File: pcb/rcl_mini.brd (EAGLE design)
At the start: 83.8 x 64.4 mm, 60 parts, among them CN1 USB mini B, Q1 8MHz, Q2 IRLML5203, U1 MCP6002T-I/SN, U2 MCP6002T-I/SN, U3 MCP6002T-I/SN, U4 STM32F100CBT6, U5 MCP73831/OT, U6 MCP1703CB, X1 BAT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

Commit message: pcb v1.0
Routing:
- net GND: track 474.3 -> 493.9 mm
- net VDD: track 138.5 -> 146.2 mm
- net HCUR: track 4.98 -> 10.8 mm
- net LCUR: track 5.10 -> 10.5 mm
- net LPOT: track 11.8 -> 16.9 mm
- net SWDIO: track 26.8 -> 31.9 mm
- net SWCLK: track 36.2 -> 41.2 mm
- net VBAT+: track 36.4 -> 40.2 mm
- net HPOT: track 11.5 -> 15.2 mm
- net OLED_I2C_SDA: track 28.3 -> 30.8 mm
- net OLED_I2C_SCK: track 34.3 -> 36.8 mm
- net UART_TX: track 24.3 -> 26.8 mm
- net UART_RX: track 24.5 -> 27.0 mm
- net SW3: track 21.0 -> 23.5 mm
- net SW1: track 25.7 -> 27.4 mm
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
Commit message: pcb v1.0 completed
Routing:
- net GND: track 493.9 -> 527.9 mm
- net HCUR2: track 17.4 -> 23.5 mm
- net USB+: track 23.2 -> 22.5 mm

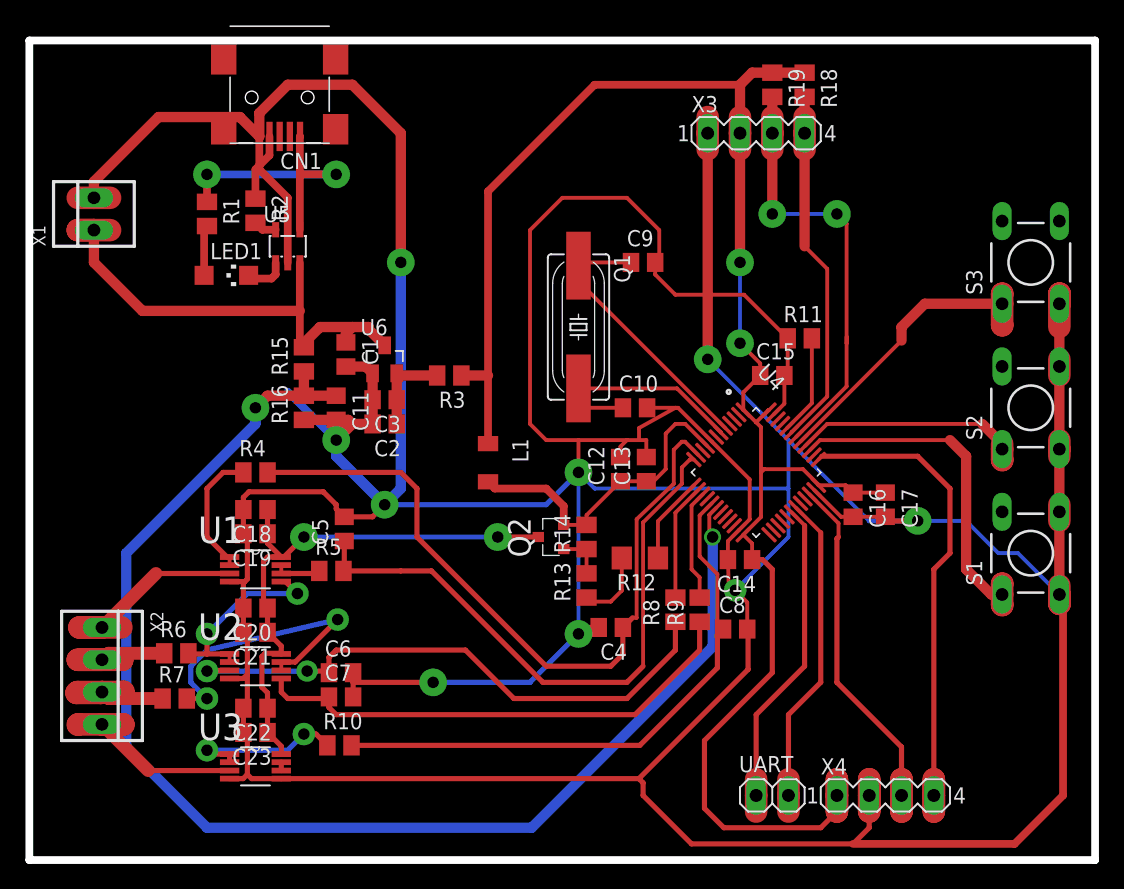
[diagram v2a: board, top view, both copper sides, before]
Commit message: mcp6002 package was changed from msop to soic
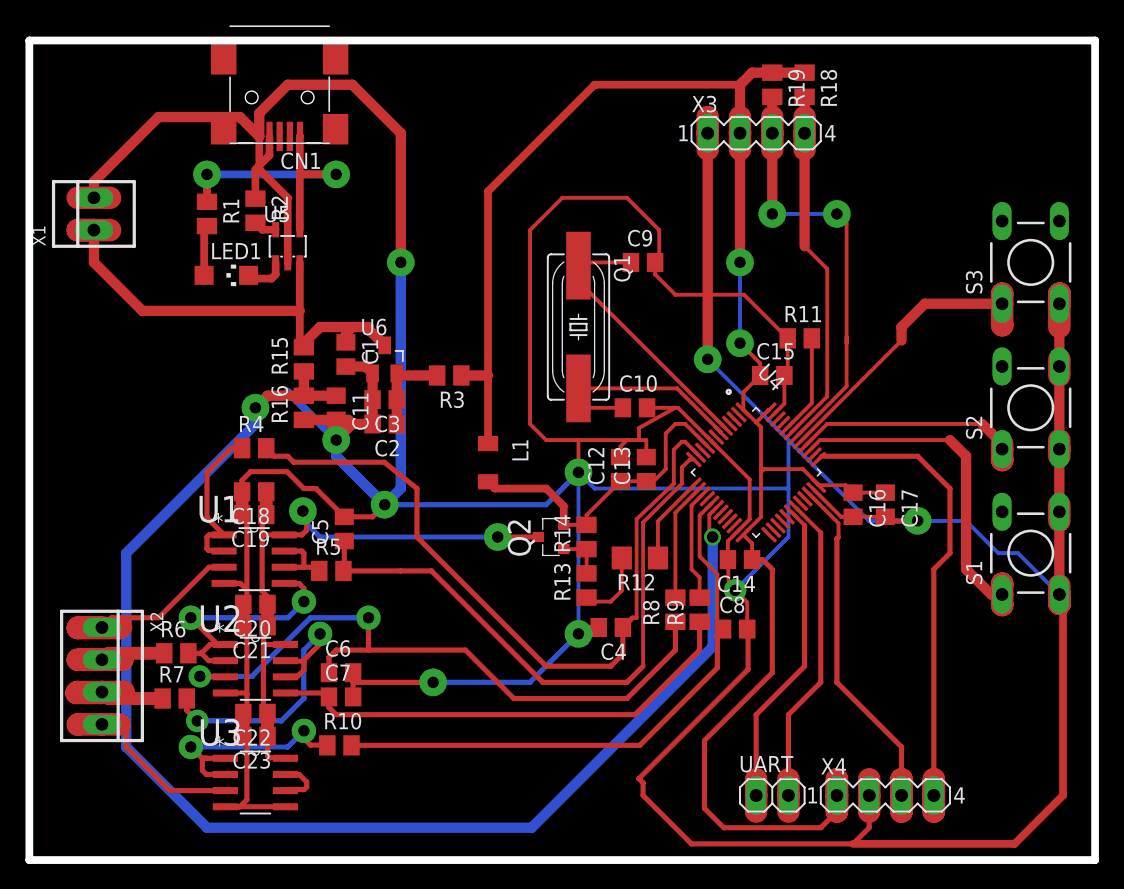
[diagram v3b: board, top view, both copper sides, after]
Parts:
- U1, U2, U3: device MCP6002T:SOP65P490X110-8N -> MCP6002:SOIC127P600X175-8N
- moved R4 1.90 mm to (26.6, 67.9)
- moved C19 1.50 mm to (26.6, 62.7)
- moved C18 1.40 mm to (26.6, 64.5)
- moved U3 1.27 mm to (26.7, 41.7)
- moved U1 0.81 mm to (26.6, 59.2)
- moved C21 0.50 mm to (26.7, 54.0)
- moved C22 0.40 mm to (26.7, 47.1)
- moved C23 0.30 mm to (26.7, 45.3)
- moved C20 0.30 mm to (26.7, 55.7)
- moved U2 0.20 mm to (26.7, 50.6)
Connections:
- net LPOT renamed N$7
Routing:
- net GND: track 527.9 -> 495.9 mm
- net N$11: track 45.5 -> 53.8 mm
- net VCC_OPAMP: track 44.4 -> 50.4 mm
- net LCUR2: track 15.6 -> 21.1 mm
- net N$19: track 12.9 -> 18.3 mm
- net N$21: track 0.66 -> 4.10 mm
- net N$6: track 10.3 -> 12.8 mm
- net N$10: track 3.73 -> 5.60 mm
- net N$16: track 39.6 -> 38.1 mm
- net PA1: track 57.5 -> 58.2 mm
- net HPOT: track 15.2 -> 15.9 mm

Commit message: pcb design improvements
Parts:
- moved R3 6.40 mm to (39.2, 67.9)
- moved C17 6.35 mm to (69.8, 63.5)
- moved U4 6.35 mm to (59.7, 66.0)
- moved X3 6.35 mm to (59.7, 92.7)
- moved X4 6.35 mm to (69.8, 40.6)
- moved C10 6.35 mm to (50.2, 71.1)
- moved C12 6.35 mm to (49.0, 66.3)
- moved C13 6.35 mm to (51.1, 66.3)
- moved C15 6.35 mm to (61.0, 73.7)
- moved C4 6.35 mm to (48.3, 53.8)
- moved C9 6.35 mm to (50.8, 82.5)
- moved Q1 6.35 mm to (45.7, 77.5)
- moved Q2 6.35 mm to (43.6, 61.0)
- moved R12 6.35 mm to (50.5, 59.3)
- moved R13 6.35 mm to (46.4, 57.1)
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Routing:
- net GND: track 495.9 -> 480.2 mm
- net VCC_OPAMP: track 50.4 -> 43.6 mm
- net N$11: track 53.8 -> 47.4 mm
- net N$16: track 38.1 -> 31.7 mm
- net PA7: track 46.9 -> 40.5 mm
- net N$20: track 105.6 -> 99.2 mm
- net VDD: track 146.2 -> 140.9 mm
- net VDDA: track 25.6 -> 21.3 mm
- net PA2: track 48.2 -> 44.1 mm
- net SWDIO: track 31.9 -> 28.1 mm
- net SWCLK: track 41.2 -> 37.4 mm
- net OLED_I2C_SCK: track 36.8 -> 33.8 mm
- net PA1: track 58.2 -> 55.6 mm
- net OLED_I2C_SDA: track 30.8 -> 28.3 mm
- net UART_RX: track 27.0 -> 25.7 mm
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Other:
- board size 83.8 x 64.4 mm -> 77.5 x 64.4 mm

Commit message: pcb design improvements
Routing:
- net GND: track 480.2 -> 478.6 mm
- net HCUR2: track 23.3 -> 22.3 mm
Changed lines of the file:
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@@
 <wire x1="49.53" y1="87.63" x2="52.07" y2="85.09" width="0.3048" layer="1"/>
 <wire x1="52.07" y1="85.09" x2="52.07" y2="82.87" width="0.3048" layer="1"/>
-<wire x1="51.75" y1="82.55" x2="52.07" y2="82.87" width="0.3048" layer="1"/>
+<wire x1="52.07" y1="82.87" x2="51.75" y2="82.55" width="0.3048" layer="1"/>
 <wire x1="41.91" y1="69.85" x2="41.91" y2="85.09" width="0.3048" layer="1"/>
 <wire x1="59.182" y1="62.35001875" x2="58.32528125" y2="61.493303125" width="0.3048" layer="1"/>
 <wire x1="59.182" y1="65.487340625" x2="56.2039625" y2="68.465375" width="0.3048" layer="1"/>
 <wire x1="59.182" y1="62.35001875" x2="59.182" y2="65.487340625" width="0.3048" layer="1"/>
-<wire x1="50.48" y1="68.58" x2="50.48" y2="69.53" width="0.3048" layer="1"/>
-<wire x1="50.48" y1="69.53" x2="51.64" y2="71.12" width="0.3048" layer="1"/>
+<wire x1="50.48" y1="68.58" x2="50.48" y2="69.53" width="0.6096" layer="1"/>
+<wire x1="50.48" y1="69.53" x2="51.64" y2="71.12" width="0.6096" layer="1"/>
 <wire x1="51.054" y1="67.244" x2="51.054" y2="68.58" width="0.3048" layer="1"/>
 <wire x1="49.022" y1="67.244" x2="49.022" y2="68.072" width="0.3048" layer="1"/>
@@
 <contactref element="S1" pad="3"/>
 <contactref element="S3" pad="3"/>
-<wire x1="55.88" y1="80.01" x2="53.34" y2="80.01" width="0.3048" layer="1"/>
-<wire x1="53.34" y1="80.01" x2="51.75" y2="81.6" width="0.3048" layer="1"/>
-<wire x1="51.75" y1="81.6" x2="51.75" y2="82.55" width="0.3048" layer="1"/>
 <wire x1="55.88" y1="80.01" x2="58.74" y2="80.01" width="0.3048" layer="1"/>
 <wire x1="58.74" y1="80.01" x2="62.169" y2="76.581" width="0.3048" layer="1"/>
@@
 <wire x1="34.351" y1="50.292" x2="34.351" y2="49.53" width="0.4064" layer="1"/>
 <wire x1="34.351" y1="49.53" x2="34.351" y2="48.387" width="0.4064" layer="1"/>
-<wire x1="34.351" y1="49.53" x2="37.1" y2="49.53" width="0.4064" layer="1"/>
-<via x="37.1" y="49.53" extent="1-16" drill="0.9" diameter="2.1844"/>
-<wire x1="37.1" y1="49.53" x2="41.91" y2="49.53" width="0.4064" layer="16"/>
+<wire x1="34.351" y1="49.53" x2="36.8" y2="49.53" width="0.4064" layer="1"/>
+<via x="36.8" y="49.53" extent="1-16" drill="0.9" diameter="2.1844"/>
+<wire x1="36.8" y1="49.53" x2="41.91" y2="49.53" width="0.4064" layer="16"/>
 <wire x1="41.91" y1="49.53" x2="45.72" y2="53.34" width="0.4064" layer="16"/>
 <wire x1="47.31" y1="53.848" x2="46.228" y2="53.848" width="0.4064" layer="1"/>
@@
 <wire x1="59.055" y1="50.546" x2="59.055" y2="53.655" width="0.4064" layer="1"/>
 <wire x1="59.055" y1="53.655" x2="58.989" y2="53.721" width="0.4064" layer="1"/>
-<wire x1="55.88" y1="91.44" x2="55.88" y2="80.01" width="0.8128" layer="1"/>
+<wire x1="55.88" y1="82.55" x2="55.88" y2="91.44" width="0.8128" layer="1"/>
+<wire x1="55.88" y1="82.55" x2="55.88" y2="80.01" width="0.8128" layer="1"/>
 <wire x1="35.88" y1="71.755" x2="35.88" y2="73.83" width="0.8128" layer="1"/>
 <wire x1="35.88" y1="71.755" x2="35.88" y2="69.85" width="0.8128" layer="1"/>
@@
 <wire x1="26" y1="56.8" x2="26" y2="62.334" width="0.4064" layer="1"/>
 <wire x1="26" y1="62.334" x2="25.62" y2="62.714" width="0.4064" layer="1"/>
+<wire x1="51.75" y1="82.55" x2="55.88" y2="82.55" width="0.6096" layer="1"/>
 </signal>
 <signal name="USB+">
@@
 <wire x1="54.112234375" y1="69.85" x2="53.34" y2="69.85" width="0.3048" layer="1"/>
 <wire x1="53.34" y1="69.85" x2="52.578" y2="69.088" width="0.3048" layer="1"/>
-<wire x1="52.578" y1="69.088" x2="52.578" y2="66.294" width="0.3048" layer="1"/>
-<wire x1="52.578" y1="66.294" x2="51.628" y2="65.344" width="0.3048" layer="1"/>
-<wire x1="51.628" y1="65.344" x2="51.054" y2="65.344" width="0.3048" layer="1"/>
-<wire x1="51.054" y1="65.344" x2="49.022" y2="65.344" width="0.3048" layer="1"/>
+<wire x1="52.578" y1="69.088" x2="52.578" y2="65.994" width="0.3048" layer="1"/>
+<wire x1="52.578" y1="65.994" x2="51.528" y2="64.944" width="0.3048" layer="1"/>
+<wire x1="51.528" y1="64.944" x2="51.054" y2="65.344" width="0.3048" layer="1"/>
+<wire x1="51.054" y1="65.344" x2="49.022" y2="65.344" width="0.8128" layer="1"/>
 <wire x1="49.022" y1="65.344" x2="46.355" y2="62.677" width="0.3048" layer="1"/>
 <wire x1="46.355" y1="62.677" x2="46.355" y2="61.91" width="0.3048" layer="1"/>
@@
 <contactref element="C19" pad="1"/>
 <contactref element="C18" pad="1"/>
-<via x="39.37" y="60.96" extent="1-16" drill="0.9" diameter="2.1844"/>
-<wire x1="39.37" y1="60.96" x2="42.561" y2="60.96" width="0.4064" layer="1"/>
+<via x="40.87" y="60.96" extent="1-16" drill="0.9" diameter="2.1844"/>
+<wire x1="40.87" y1="60.96" x2="42.561" y2="60.96" width="0.4064" layer="1"/>
 <wire x1="27.62" y1="47.098" x2="27.62" y2="45.293" width="1.016" layer="1"/>
 <wire x1="27.62" y1="45.293" x2="27.62" y2="43.78" width="0.4064" layer="1"/>
@@
 <via x="30.4" y="63" extent="1-16" drill="0.9" diameter="2.1844"/>
 <wire x1="30.4" y1="62.31" x2="30.4" y2="63" width="0.4064" layer="16"/>
-<wire x1="39.37" y1="60.96" x2="31.75" y2="60.96" width="0.4064" layer="16"/>
+<wire x1="40.87" y1="60.96" x2="31.75" y2="60.96" width="0.4064" layer="16"/>
 <wire x1="31.75" y1="60.96" x2="30.4" y2="62.31" width="0.4064" layer="16"/>
 <wire x1="29.0322" y1="52.505" x2="27.495" y2="52.505" width="0.4064" layer="1"/>
@@
 <wire x1="53.848" y1="68.453" x2="53.213" y2="67.818" width="0.3048" layer="1"/>
 <wire x1="53.213" y1="65.151" x2="50.292" y2="62.357" width="0.3048" layer="1"/>
-<wire x1="50.292" y1="62.357" x2="50.292" y2="54.61" width="0.3048" layer="1"/>
+<wire x1="50.292" y1="62.357" x2="50.292" y2="54.91" width="0.3048" layer="1"/>
 <wire x1="53.213" y1="67.818" x2="53.213" y2="65.151" width="0.3048" layer="1"/>
-<wire x1="50.292" y1="54.61" x2="49.972" y2="54.61" width="0.3048" layer="1"/>
+<wire x1="50.292" y1="54.91" x2="49.972" y2="54.61" width="0.3048" layer="1"/>
 <wire x1="49.972" y1="54.61" x2="49.21" y2="53.848" width="0.4064" layer="1"/>
 <wire x1="49.21" y1="53.848" x2="49.21" y2="51.75" width="0.4064" layer="1"/>
@@
 <wire x1="22.1" y1="46.5" x2="28.72" y2="46.5" width="0.4064" layer="16"/>
 <wire x1="28.72" y1="46.5" x2="30.48" y2="48.26" width="0.4064" layer="16"/>
-<wire x1="30.48" y1="48.26" x2="30.48" y2="52.07" width="0.4064" layer="16"/>
-<wire x1="30.48" y1="52.07" x2="31.75" y2="53.34" width="0.4064" layer="16"/>
-<via x="31.75" y="53.34" extent="1-16" drill="0.9" diameter="1.9304"/>
-<wire x1="31.75" y1="53.34" x2="31.75" y2="52.55" width="0.4064" layer="1"/>
+<wire x1="30.48" y1="48.26" x2="30.48" y2="51.57" width="0.4064" layer="16"/>
+<wire x1="30.48" y1="51.57" x2="31.75" y2="52.84" width="0.4064" layer="16"/>
+<via x="31.75" y="52.84" extent="1-16" drill="0.9" diameter="1.9304"/>
+<wire x1="31.75" y1="52.84" x2="31.75" y2="52.55" width="0.4064" layer="1"/>
 <wire x1="30.4" y1="51.2" x2="31.75" y2="52.55" width="0.4064" layer="1"/>
 <wire x1="30.4" y1="51.2" x2="29.0672" y2="51.2" width="0.4064" layer="1"/>
@@
 <wire x1="57.264621875" y1="69.526034375" x2="45.72" y2="81.070659375" width="0.3048" layer="1"/>
 <wire x1="45.72" y1="82.296" x2="45.72" y2="81.070659375" width="0.3048" layer="1"/>
-<wire x1="49.85" y1="82.55" x2="45.974" y2="82.55" width="0.3048" layer="1"/>
+<wire x1="49.85" y1="82.55" x2="45.974" y2="82.55" width="0.8128" layer="1"/>
 <wire x1="45.974" y1="82.55" x2="45.72" y2="82.296" width="0.3048" layer="1"/>
 </signal>
@@
 <wire x1="45.72" y1="72.644" x2="53.467" y2="72.644" width="0.3048" layer="1"/>
 <wire x1="56.911071875" y1="69.199928125" x2="53.467" y2="72.644" width="0.3048" layer="1"/>
-<wire x1="49.215" y1="71.12" x2="45.72" y2="71.12" width="0.3048" layer="1"/>
+<wire x1="49.215" y1="71.12" x2="45.72" y2="71.12" width="0.8128" layer="1"/>
 <wire x1="45.72" y1="71.12" x2="45.72" y2="72.644" width="0.3048" layer="1"/>
 </signal>
